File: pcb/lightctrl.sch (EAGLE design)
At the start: 30 parts, among them IC1 AtMega644A/1284, K1 AQY2212VEHA, Q1 3.6864MHz, X1 ISP/UART

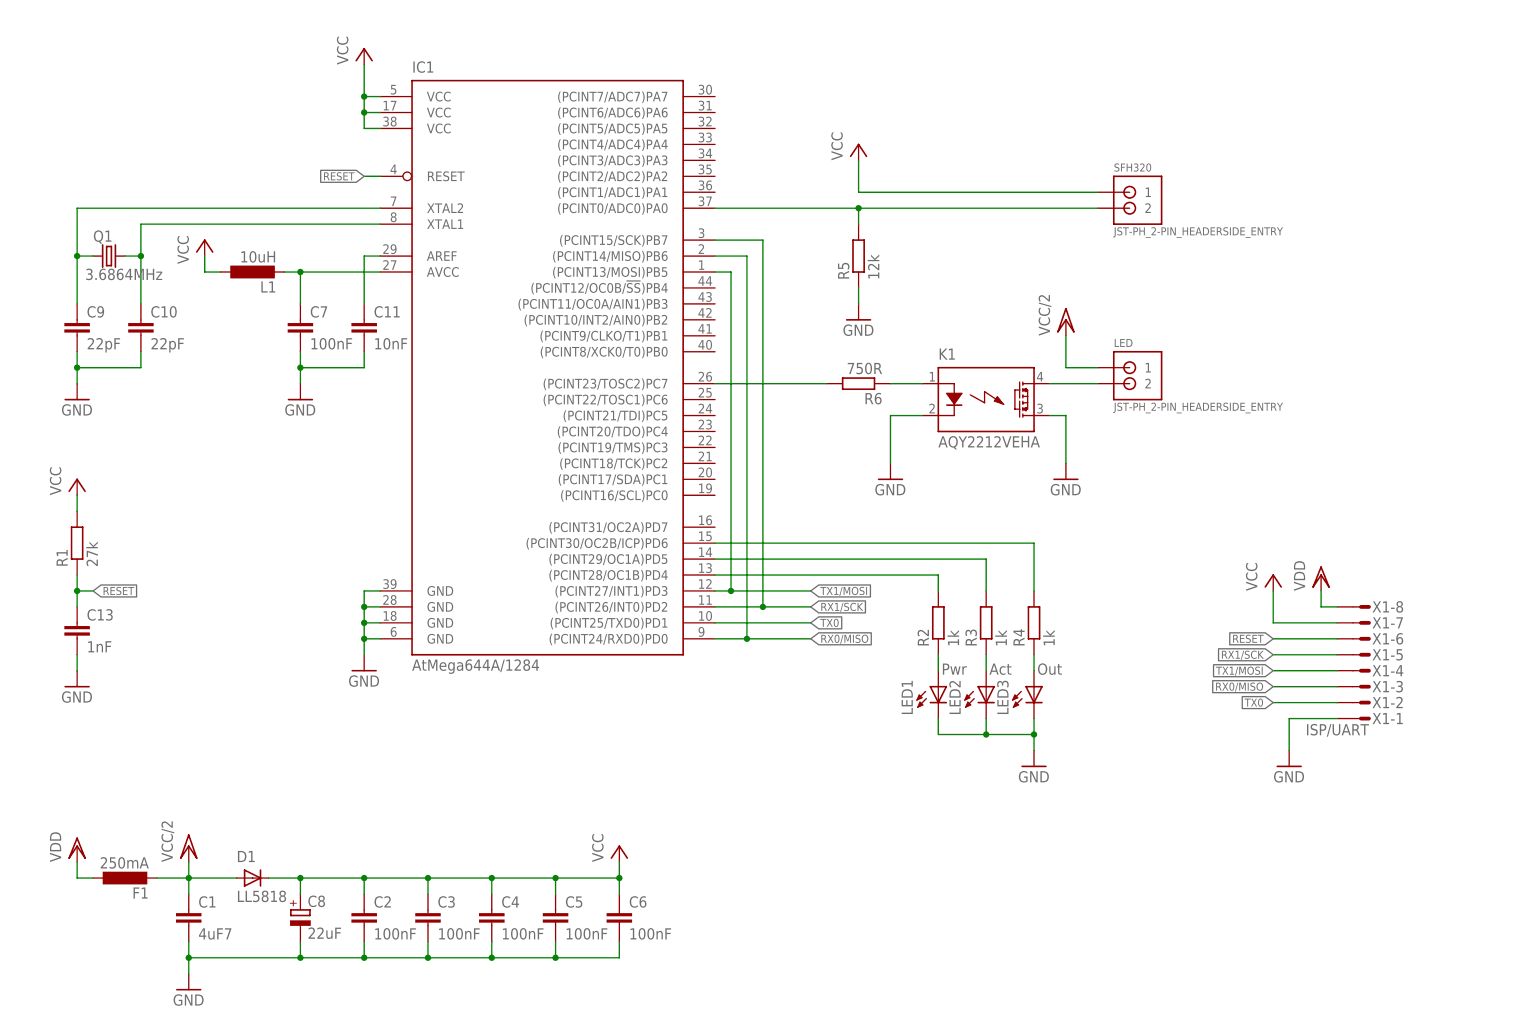
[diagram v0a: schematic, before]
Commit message: Update pcb and documentation to rev.B: fix padsize for D1, add gpio protection for MCU, slightly widen board to get better grip in battery compartment
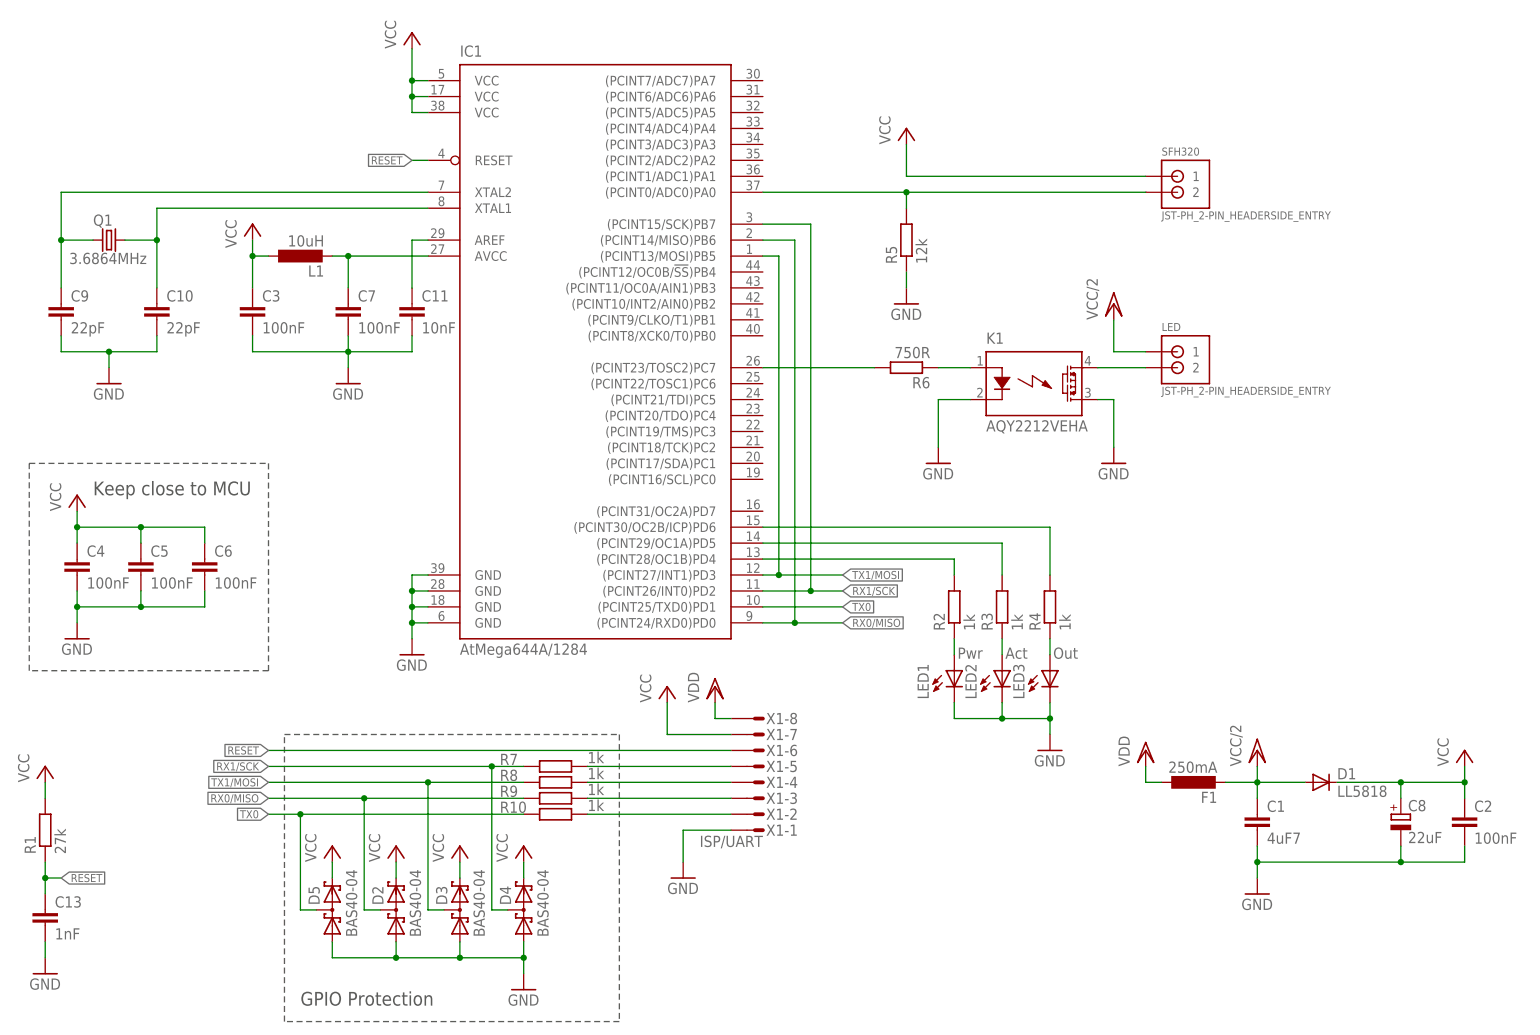
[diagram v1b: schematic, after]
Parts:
- added D2, D3, D4, D5: BAS40-04, diode:BAS40-04
- added R10, R7, R8, R9: 1k, rcl:R-EU_R1206
- D1: device diode:GF1 -> diode:DIODE-MELF-MLL41
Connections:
- new net N$13: R7.2, X1-5.S
- new net N$15: R8.2, X1-4.S
- new net N$16: R9.2, X1-3.S
- new net N$18: R10.2, X1-2.S
- net GND: now also D2.A1, D3.A1, D4.A1, D5.A1
- net RX0/MISO: now also D2.C1A2, R9.1; no longer X1-3.S
- net RX1/SCK: now also D4.C1A2, R7.1; no longer X1-5.S
- net TX0: now also D5.C1A2, R10.1; no longer X1-2.S
- net TX1/MOSI: now also D3.C1A2, R8.1; no longer X1-4.S
- net VCC: now also D2.C2, D3.C2, D4.C2, D5.C2
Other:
- note added: "GPIO Protection"
- note added: "Keep close to MCU"
- moved on the sheet: C1, C10, C11, C13, C2, C3, C4, C5, C6, C7, C8, C9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
